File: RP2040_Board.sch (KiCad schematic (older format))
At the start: 9 parts, among them J1 V_OUT, J2 mA_OUT, J3 mA_IN, J4 V_IN, J5 DIG_OUT, J6 DIG_OUT, U2 Pico

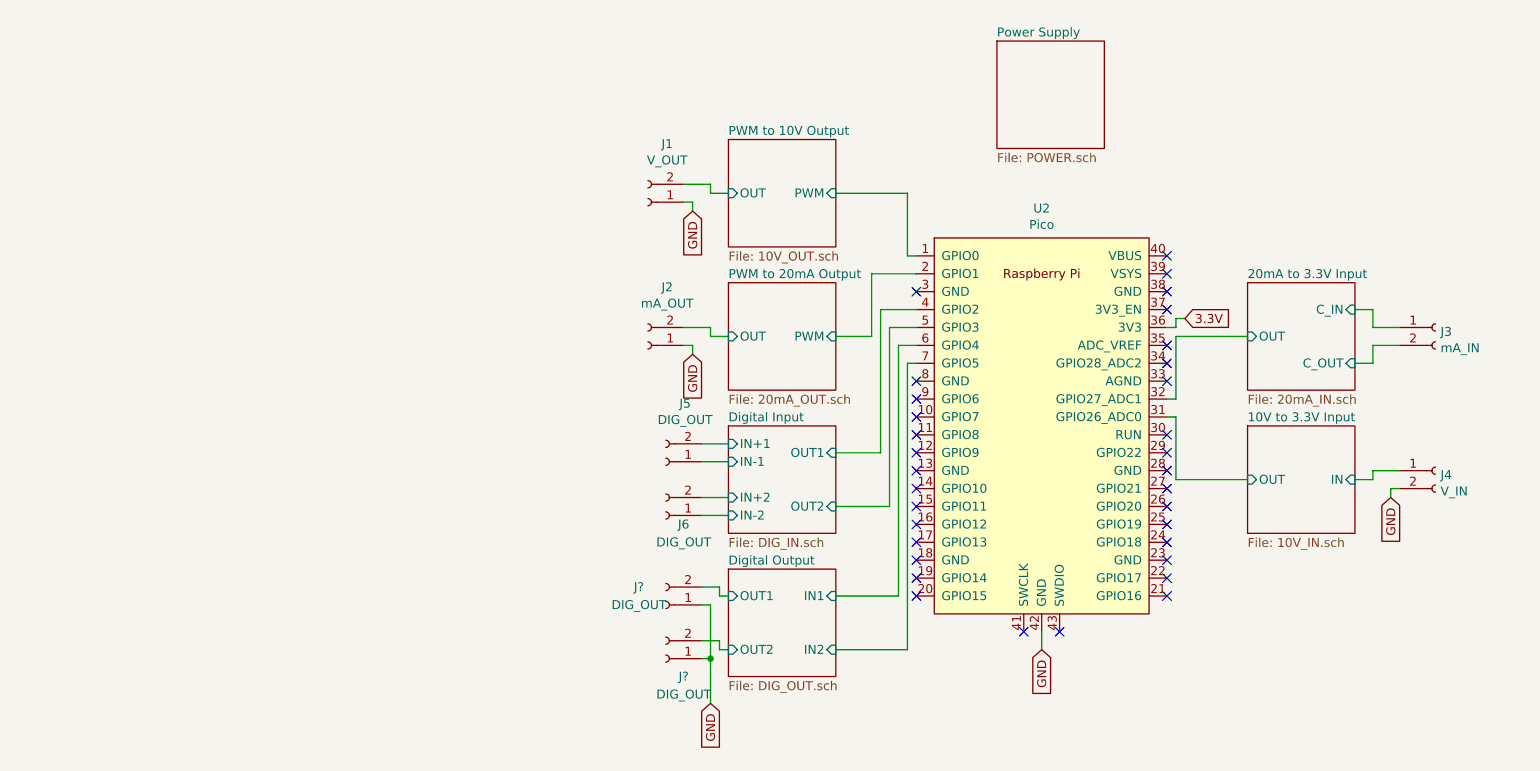
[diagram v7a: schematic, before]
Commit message: Footprint Association
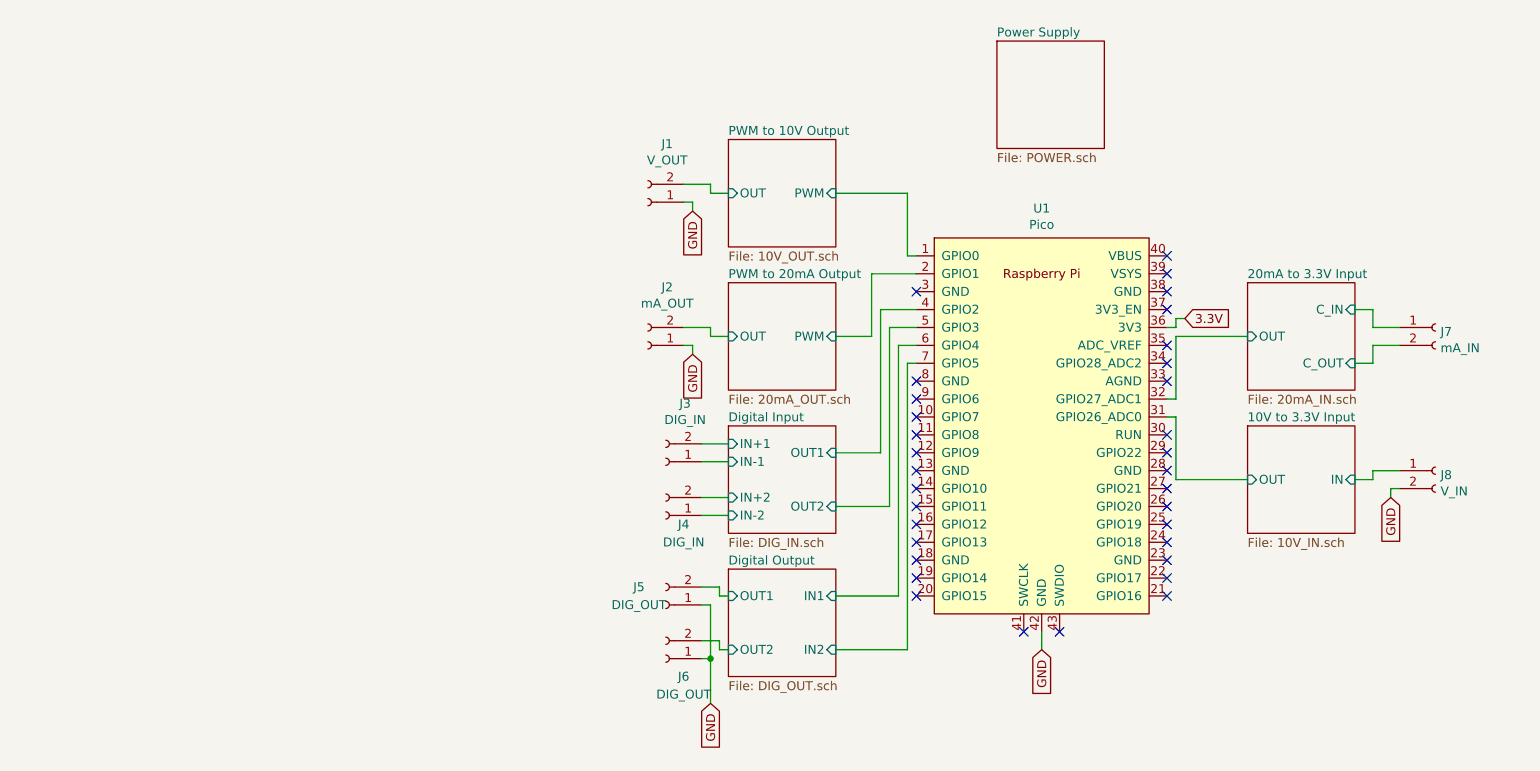
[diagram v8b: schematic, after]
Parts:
- J3: renamed from J5; value DIG_OUT -> DIG_IN
- J4: renamed from J6; value DIG_OUT -> DIG_IN
- J7: renamed from J3; footprint Connector_PinSocket_1.00mm:PinSocket_1x02_P1.00mm_Vertical -> (none)
- gave numbers to parts that had none: 2
- renumbered J4 to J8, U2 to U1
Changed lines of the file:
@@
 $EndDescr
 $Comp
-L MCU_RaspberryPi_and_Boards:Pico U2
+L MCU_RaspberryPi_and_Boards:Pico U1
 U 1 1 60A8B6FD
 P 5900 4100
-F 0 "U2" H 5900 5315 50  0000 C CNN
+F 0 "U1" H 5900 5315 50  0000 C CNN
 F 1 "Pico" H 5900 5224 50  0000 C CNN
 F 2 "MCU_RaspberryPi_and_Boards:RPi_Pico_SMD_TH" V 5900 4100 50  0001 C CNN
@@
 NoConn ~ 6600 5050
 $Comp
-L Connector:Conn_01x02_Female J3
+L Connector:Conn_01x02_Female J7
 U 1 1 60AFC2F2
 P 8100 3550
-F 0 "J3" H 8128 3526 50  0000 L CNN
+F 0 "J7" H 8128 3526 50  0000 L CNN
 F 1 "mA_IN" H 8128 3435 50  0000 L CNN
-F 2 "Connector_PinSocket_1.00mm:PinSocket_1x02_P1.00mm_Vertical" H 8100 3550 50  0001 C CNN
+F 2 "" H 8100 3550 50  0001 C CNN
 F 3 "~" H 8100 3550 50  0001 C CNN
 	1    8100 3550
@@
 $EndSheet
 $Comp
-L Connector:Conn_01x02_Female J4
+L Connector:Conn_01x02_Female J8
 U 1 1 60B06785
 P 8100 4350
-F 0 "J4" H 8128 4326 50  0000 L CNN
+F 0 "J8" H 8128 4326 50  0000 L CNN
 F 1 "V_IN" H 8128 4235 50  0000 L CNN
 F 2 "" H 8100 4350 50  0001 C CNN
@@
 3.3V
 $Comp
-L Connector:Conn_01x02_Female J5
+L Connector:Conn_01x02_Female J3
 U 1 1 60B47D03
 P 3800 4300
-F 0 "J5" H 3692 3975 50  0000 C CNN
-F 1 "DIG_OUT" H 3692 4066 50  0000 C CNN
+F 0 "J3" H 3692 3975 50  0000 C CNN
+F 1 "DIG_IN" H 3692 4066 50  0000 C CNN
 F 2 "" H 3800 4300 50  0001 C CNN
 F 3 "~" H 3800 4300 50  0001 C CNN
@@
 	6650 3500 6700 3500
 $Comp
-L Connector:Conn_01x02_Female J6
+L Connector:Conn_01x02_Female J4
 U 1 1 60BADF7F
 P 3800 4600
-F 0 "J6" H 3700 4650 50  0000 C CNN
-F 1 "DIG_OUT" H 3700 4750 50  0000 C CNN
+F 0 "J4" H 3700 4650 50  0000 C CNN
+F 1 "DIG_IN" H 3700 4750 50  0000 C CNN
 F 2 "" H 3800 4600 50  0001 C CNN
 F 3 "~" H 3800 4600 50  0001 C CNN
@@
 	4950 3600 4750 3600
 $Comp
-L Connector:Conn_01x02_Female J?
+L Connector:Conn_01x02_Female J5
 U 1 1 60C380A7
 P 3800 5100
-F 0 "J?" H 3950 5000 50  0000 C CNN
+F 0 "J5" H 3950 5000 50  0000 C CNN
 F 1 "DIG_OUT" H 3950 5100 50  0000 C CNN
 F 2 "" H 3800 5100 50  0001 C CNN
@@
 $EndComp
 $Comp
-L Connector:Conn_01x02_Female J?
+L Connector:Conn_01x02_Female J6
 U 1 1 60C39103
 P 3800 5400
-F 0 "J?" H 3700 5500 50  0000 C CNN
+F 0 "J6" H 3700 5500 50  0000 C CNN
 F 1 "DIG_OUT" H 3700 5600 50  0000 C CNN
 F 2 "" H 3800 5400 50  0001 C CNN
